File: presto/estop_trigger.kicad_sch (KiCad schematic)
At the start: 0 parts

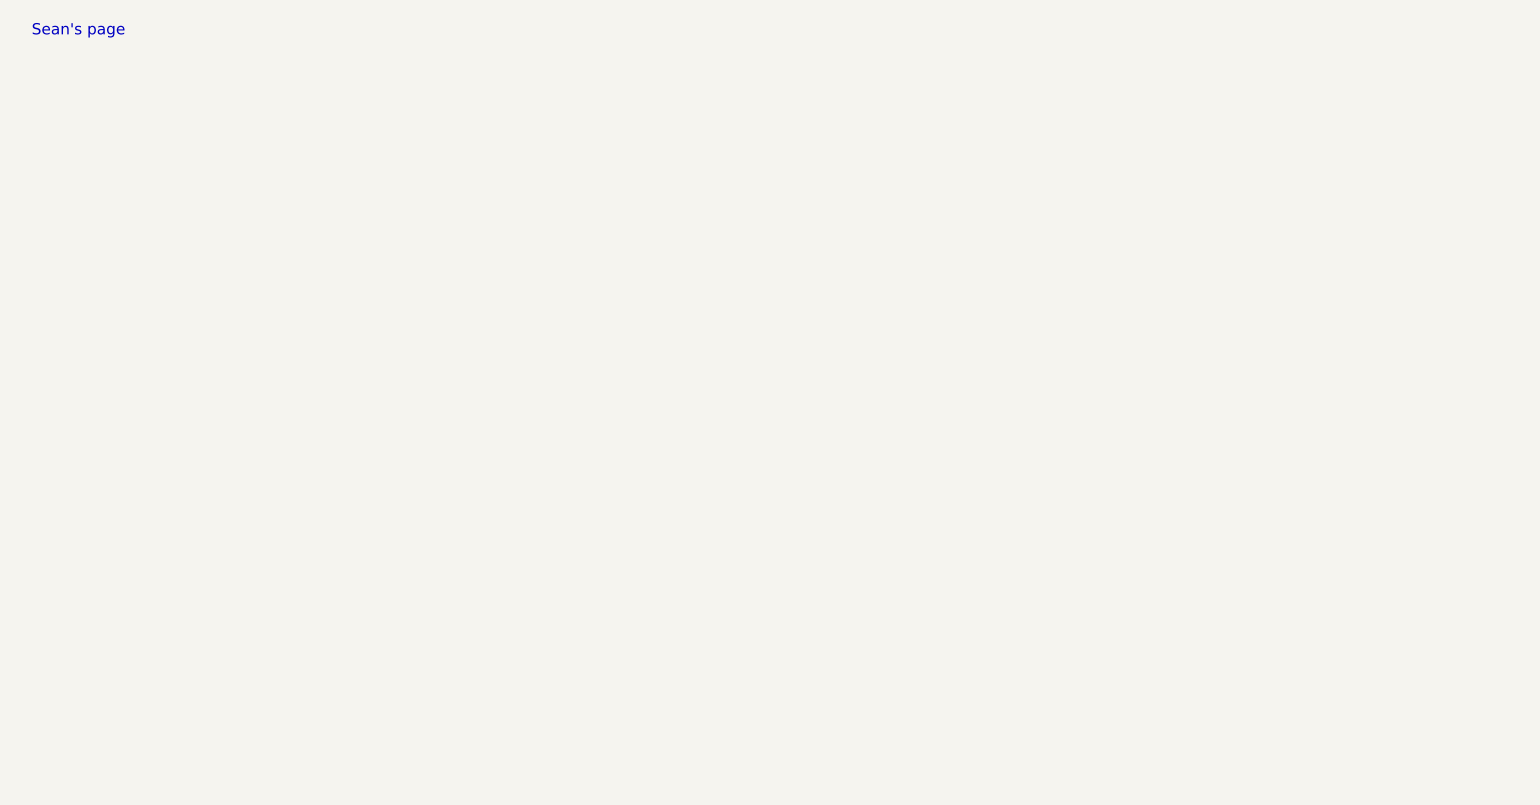
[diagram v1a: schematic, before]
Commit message: Added estop, power, led schematics
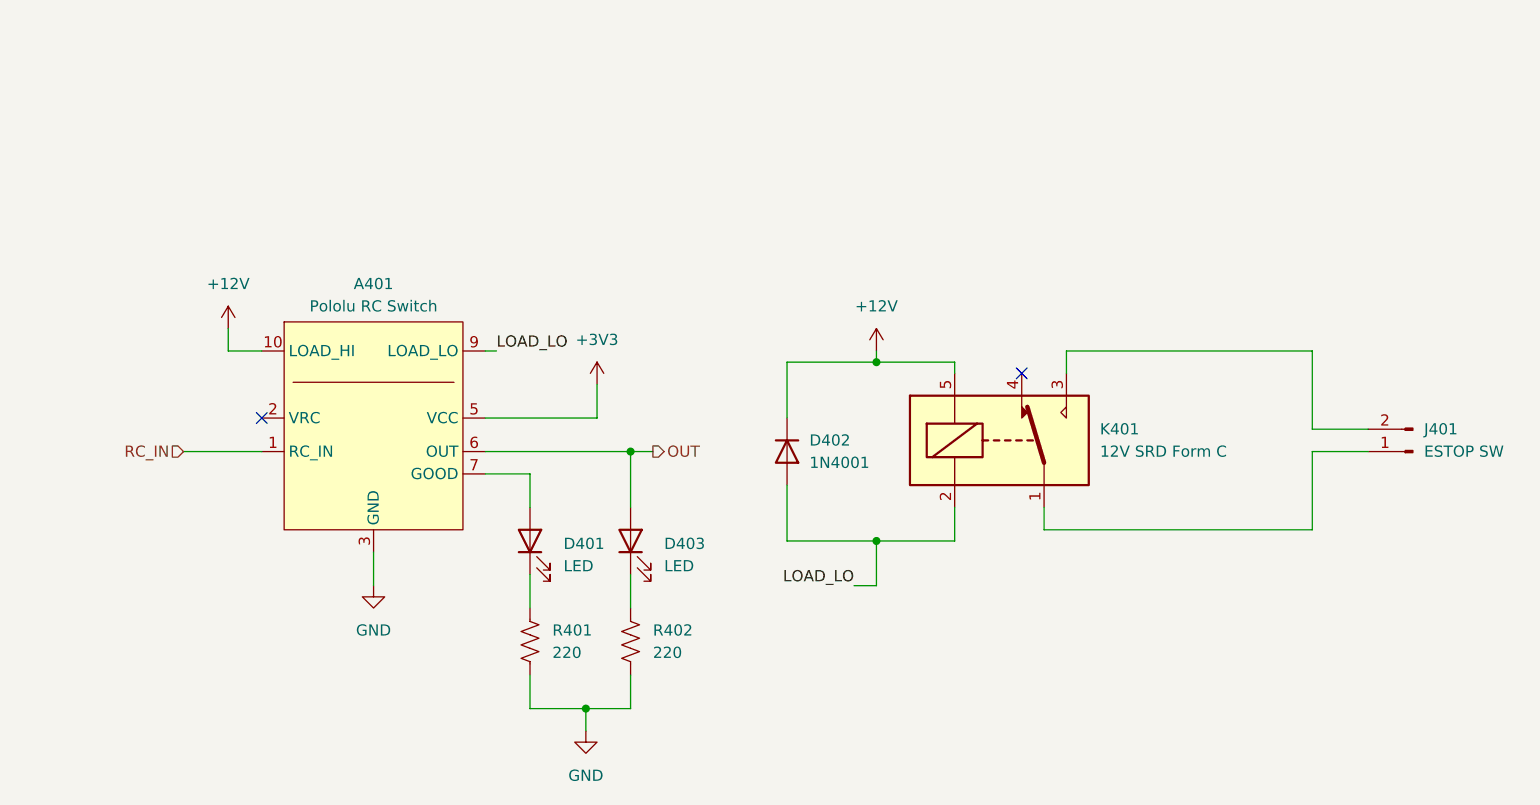
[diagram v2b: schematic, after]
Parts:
- added A401: Pololu RC Switch, GTMRG_Footprints:Pololu_2802_RCSw, symbol GTMRG_Boards:Pololu_2802_RCSw
- added D401, D403: LED, LED_SMD:LED_1206_3216Metric_Pad1.42x1.75mm_HandSolder, symbol Device:LED
- added D402: 1N4001, Diode_THT:D_DO-41_SOD81_P10.16mm_Horizontal, symbol Diode:1N4001
- added J401: ESTOP SW, Connector_AMASS:AMASS_XT30PW-M_1x02_P2.50mm_Horizontal, symbol Connector:Conn_01x02_Pin
- added K401: 12V SRD Form C, Relay_THT:Relay_SPDT_SANYOU_SRD_Series_Form_C, symbol Relay:SANYOU_SRD_Form_C
- added R401, R402: 220, Resistor_SMD:R_1206_3216Metric_Pad1.30x1.75mm_HandSolder, symbol Device:R_US
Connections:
- new net: D403.1 (K), R402.1
- new net: J401.1 (Pin_1), K401.1
- new net: J401.2 (Pin_2), K401.3
- new net: A401.7 (GOOD), D401.2 (A)
- new net: D401.1 (K), R401.1
- new net +12V: A401.10 (LOAD_HI), A401.11 (LOAD_HI), D402.1 (K), K401.5
- new net +3V3: A401.5 (VCC)
- new net GND: A401.3 (GND), A401.4 (GND), A401.8 (GND), R401.2, R402.2
- new net LOAD_LO: A401.9 (LOAD_LO), D402.2 (A), K401.2
- new net OUT: A401.6 (OUT), D403.2 (A)
- new net RC_IN: A401.1 (RC_IN)
- no-connect marks 0 -> 2
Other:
- note removed: "Sean's page"

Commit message: Presto PCB edited with schematic, components placed, wiring in progress
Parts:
- renumbered D403 to D402, D402 to D403
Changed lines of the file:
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@@
 		(dnp no)
 		(fields_autoplaced yes)
-		(property "Reference" "D402"
+		(property "Reference" "D403"
 			(at 148.59 95.2499 90)
 			(effects
@@
 			(project "presto"
 				(path "/0fac30c0-3f82-4ab4-8888-b9c60b2e0ca9/77affc6e-f265-4557-b7a6-ffe1a5f06898"
-					(reference "D402")
+					(reference "D403")
 					(unit 1)
 				)
@@
 		(dnp no)
 		(fields_autoplaced yes)
-		(property "Reference" "#PWR0401"
+		(property "Reference" "#PWR0402"
 			(at 99.06 118.11 0)
 			(effects
@@
 			(project "presto"
 				(path "/0fac30c0-3f82-4ab4-8888-b9c60b2e0ca9/77affc6e-f265-4557-b7a6-ffe1a5f06898"
-					(reference "#PWR0401")
+					(reference "#PWR0402")
 					(unit 1)
 				)
@@
 		(dnp no)
 		(fields_autoplaced yes)
-		(property "Reference" "#PWR0404"
+		(property "Reference" "#PWR0403"
 			(at 123.19 134.62 0)
 			(effects
@@
 			(project "presto"
 				(path "/0fac30c0-3f82-4ab4-8888-b9c60b2e0ca9/77affc6e-f265-4557-b7a6-ffe1a5f06898"
-					(reference "#PWR0404")
+					(reference "#PWR0403")
 					(unit 1)
 				)
@@
 		(dnp no)
 		(fields_autoplaced yes)
-		(property "Reference" "#PWR0403"
+		(property "Reference" "#PWR0401"
 			(at 82.55 86.36 0)
 			(effects
@@
 			(project ""
 				(path "/0fac30c0-3f82-4ab4-8888-b9c60b2e0ca9/77affc6e-f265-4557-b7a6-ffe1a5f06898"
-					(reference "#PWR0403")
+					(reference "#PWR0401")
 					(unit 1)
 				)
@@
 		(dnp no)
 		(fields_autoplaced yes)
-		(property "Reference" "#PWR0402"
+		(property "Reference" "#PWR0404"
 			(at 124.46 92.71 0)
 			(effects
@@
 			(project "presto"
 				(path "/0fac30c0-3f82-4ab4-8888-b9c60b2e0ca9/77affc6e-f265-4557-b7a6-ffe1a5f06898"
-					(reference "#PWR0402")
+					(reference "#PWR0404")
 					(unit 1)
 				)
@@
 		(dnp no)
 		(fields_autoplaced yes)
-		(property "Reference" "D403"
+		(property "Reference" "D402"
 			(at 132.08 106.9974 90)
 			(effects
@@
 			(project "presto"
 				(path "/0fac30c0-3f82-4ab4-8888-b9c60b2e0ca9/77affc6e-f265-4557-b7a6-ffe1a5f06898"
-					(reference "D403")
-					(unit 1)
-				)
+					(reference "D402")
+					(unit 1)
+				)

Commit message: added fuse and changed revision number
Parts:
- added F401: Fuse, Fuse:Fuseholder_Blade_Mini_Keystone_3568, symbol Device:Fuse
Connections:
- net at K401.3: now also F401.1; no longer J401.2 (Pin_2)
- new net: F401.2, J401.2 (Pin_2)
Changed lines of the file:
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@@
+	(wire
+		(pts
+			(xy 177.8 85.09) (xy 186.69 85.09)
+		)
+		(stroke
+			(width 0)
+			(type default)
+		)
+	)
 	(wire
 		(pts
@@
 	(wire
 		(pts
+			(xy 194.31 85.09) (xy 205.74 85.09)
+		)
+		(stroke
+			(width 0)
+			(type default)
+		)
+	)
+	(wire
+		(pts
 			(xy 175.26 105.41) (xy 205.74 105.41)
 		)
@@
 		(pts
 			(xy 82.55 82.55) (xy 82.55 85.09)
-		)
-		(stroke
-			(width 0)
-			(type default)
-		)
-	)
-	(wire
-		(pts
-			(xy 205.74 85.09) (xy 177.8 85.09)
 		)
 		(stroke
@@
 					(unit 1)
 				)
+			)
+		)
+	)
+	(symbol
+		(lib_id "Device:Fuse")
+		(at 190.5 85.09 90)
+		(unit 1)
+		(exclude_from_sim no)
+		(in_bom yes)
+		(on_board yes)
+		(dnp no)
+		(fields_autoplaced yes)
+		(property "Reference" "F401"
+			(at 190.5 78.74 90)
+			(effects
+				(font
+					(size 1.27 1.27)
+				)
+			)
+		)
+		(property "Value" "Fuse"
+			(at 190.5 81.28 90)
+			(effects
+				(font
+					(size 1.27 1.27)
+				)
+			)
+		)
+		(property "Footprint" "Fuse:Fuseholder_Blade_Mini_Keystone_3568"
+			(at 190.5 86.868 90)
+			(effects
+				(font
+					(size 1.27 1.27)
+				)
+				(hide yes)
+			)
+		)
+		(property "Datasheet" "~"
+			(at 190.5 85.09 0)
+			(effects
+				(font
+					(size 1.27 1.27)
+				)
+				(hide yes)
+			)
+		)
+		(property "Description" "Fuse"
+			(at 190.5 85.09 0)
+			(effects
+				(font
+					(size 1.27 1.27)
+				)
+				(hide yes)
+			)
+		)
+		(pin "2"
+		)
+		(pin "1"
+		)
+		(instances
+			(project ""
+				(path "/0fac30c0-3f82-4ab4-8888-b9c60b2e0ca9/77affc6e-f265-4557-b7a6-ffe1a5f06898"
+					(reference "F401")
+					(unit 1)
+				)
